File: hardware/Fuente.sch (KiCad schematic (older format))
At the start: 4 parts, among them P3 CONN_01X02, U4 NCP1117ST33T3G

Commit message: Se agrego SD, se colocaron pins en varios modulos, se corrigio orden del VGA
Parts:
- removed P3: CONN_01X02, symbol CONN_01X02
- removed U4: NCP1117ST33T3G, symbol NCP1117ST33T3G
- added U?: MCP1825S-3302E, SOT-223, symbol LM117H
- C13: value C -> 4.7uF
- C14: value C -> 1uF
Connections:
- net labels added: 3.3V_OUT, VIN
- net labels removed: +3.3V
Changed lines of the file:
@@
 LIBS:serial
 LIBS:oscillator-cmos-out-4
+LIBS:con-yamaichi-cf-2
 LIBS:STM32F4-UCC-cache
 EELAYER 24 0
@@
 $Descr A4 11693 8268
 encoding utf-8
-Sheet 5 5
+Sheet 5 6
 Title ""
 Date ""
@@
 $EndDescr
 $Comp
-L NCP1117ST33T3G U4
-U 1 1 53D551F1
-P 5350 2300
-F 0 "U4" H 5350 2550 40  0000 C CNN
-F 1 "NCP1117ST33T3G" H 5350 2500 40  0000 C CNN
-F 2 "" H 5350 2300 60  0000 C CNN
-F 3 "" H 5350 2300 60  0000 C CNN
-	1    5350 2300
-	1    0    0    -1
-$EndComp
-$Comp
 L C C14
 U 1 1 53D55294
 P 5900 2550
 F 0 "C14" H 5900 2650 40  0000 L CNN
-F 1 "C" H 5906 2465 40  0000 L CNN
+F 1 "1uF" H 5906 2465 40  0000 L CNN
 F 2 "" H 5938 2400 30  0000 C CNN
 F 3 "" H 5900 2550 60  0000 C CNN
@@
 P 4750 2550
 F 0 "C13" H 4750 2650 40  0000 L CNN
-F 1 "C" H 4756 2465 40  0000 L CNN
+F 1 "4.7uF" H 4756 2465 40  0000 L CNN
 F 2 "" H 4788 2400 30  0000 C CNN
 F 3 "" H 4750 2550 60  0000 C CNN
@@
 	1    0    0    -1
 $EndComp
-$Comp
-L CONN_01X02 P3
-U 1 1 53D55308
-P 4250 2300
-F 0 "P3" H 4250 2450 50  0000 C CNN
-F 1 "CONN_01X02" V 4350 2300 50  0000 C CNN
-F 2 "" H 4250 2300 60  0000 C CNN
-F 3 "" H 4250 2300 60  0000 C CNN
-	1    4250 2300
-	-1   0    0    1
-$EndComp
 Wire Wire Line
-	4450 2250 4950 2250
-$Comp
-L GND #PWR51
-U 1 1 53D55395
-P 4550 2450
-F 0 "#PWR51" H 4550 2450 30  0001 C CNN
-F 1 "GND" H 4550 2380 30  0001 C CNN
-F 2 "" H 4550 2450 60  0000 C CNN
-F 3 "" H 4550 2450 60  0000 C CNN
-	1    4550 2450
-	1    0    0    -1
-$EndComp
+	4550 2250 4750 2250
 Wire Wire Line
-	4450 2350 4550 2350
-Wire Wire Line
-	4550 2350 4550 2450
+	4750 2250 4950 2250
 Wire Wire Line
 	5750 2250 5900 2250
 Wire Wire Line
-	5900 2200 5900 2350
+	5900 2250 6100 2250
 Wire Wire Line
 	4750 2350 4750 2250
@@
 L GND #PWR52
 U 1 1 53D555A6
-P 4750 2850
-F 0 "#PWR52" H 4750 2850 30  0001 C CNN
-F 1 "GND" H 4750 2780 30  0001 C CNN
-F 2 "" H 4750 2850 60  0000 C CNN
-F 3 "" H 4750 2850 60  0000 C CNN
-	1    4750 2850
+P 4750 2800
+F 0 "#PWR52" H 4750 2800 30  0001 C CNN
+F 1 "GND" H 4750 2730 30  0001 C CNN
+F 2 "" H 4750 2800 60  0000 C CNN
+F 3 "" H 4750 2800 60  0000 C CNN
+	1    4750 2800
 	1    0    0    -1
 $EndComp
 Wire Wire Line
-	4750 2850 4750 2750
+	4750 2800 4750 2750
 $Comp
 L GND #PWR55
 U 1 1 53D555D6
-P 5900 2850
-F 0 "#PWR55" H 5900 2850 30  0001 C CNN
-F 1 "GND" H 5900 2780 30  0001 C CNN
-F 2 "" H 5900 2850 60  0000 C CNN
-F 3 "" H 5900 2850 60  0000 C CNN
-	1    5900 2850
+P 5900 2800
+F 0 "#PWR55" H 5900 2800 30  0001 C CNN
+F 1 "GND" H 5900 2730 30  0001 C CNN
+F 2 "" H 5900 2800 60  0000 C CNN
+F 3 "" H 5900 2800 60  0000 C CNN
+	1    5900 2800
 	1    0    0    -1
 $EndComp
 Wire Wire Line
-	5900 2850 5900 2750
+	5900 2800 5900 2750
 $Comp
 L GND #PWR53
 U 1 1 53D55626
-P 5350 2650
-F 0 "#PWR53" H 5350 2650 30  0001 C CNN
-F 1 "GND" H 5350 2580 30  0001 C CNN
-F 2 "" H 5350 2650 60  0000 C CNN
-F 3 "" H 5350 2650 60  0000 C CNN
-	1    5350 2650
+P 5350 2800
+F 0 "#PWR53" H 5350 2800 30  0001 C CNN
+F 1 "GND" H 5350 2730 30  0001 C CNN
+F 2 "" H 5350 2800 60  0000 C CNN
+F 3 "" H 5350 2800 60  0000 C CNN
+	1    5350 2800
 	1    0    0    -1
 $EndComp
 Wire Wire Line
-	5350 2650 5350 2550
+	5350 2800 5350 2550
+Connection ~ 5900 2250
 $Comp
-L +3.3V #PWR54
-U 1 1 53D55633
-P 5900 2200
-F 0 "#PWR54" H 5900 2160 30  0001 C CNN
-F 1 "+3.3V" H 5900 2310 30  0000 C CNN
-F 2 "" H 5900 2200 60  0000 C CNN
-F 3 "" H 5900 2200 60  0000 C CNN
-	1    5900 2200
+L LM117H U?
+U 1 1 53DE486A
+P 5350 2300
+F 0 "U?" H 5150 2100 40  0000 C CNN
+F 1 "MCP1825S-3302E" H 5100 2500 40  0000 L CNN
+F 2 "SOT-223" H 5350 2400 30  0000 C CIN
+F 3 "" H 5350 2300 60  0000 C CNN
+	1    5350 2300
 	1    0    0    -1
 $EndComp
-Connection ~ 5900 2250
+Text HLabel 6100 2250 2    40   Input ~ 0
+3.3V_OUT
+Wire Wire Line
+	5900 2350 5900 2250
+Text HLabel 4550 2250 0    40   Input ~ 0
+VIN
 $EndSCHEMATC

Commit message: Terminado el esquematico, iniciado el PCB
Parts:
- removed U?: MCP1825S-3302E, SOT-223, symbol LM117H
- added U4: MSP1825S-3302E, SMD_Packages:SOT-223, symbol MSP1825S-3302E
- C13, C14: footprint (none) -> Capacitors_ThroughHole:Capacitor5x11RM2.5
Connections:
- net 3.3V_OUT: now also U4.3 (OUT)
- net GND: now also U4.2 (ADJ), U4.4 (gnd)
- net VIN: now also U4.1 (IN)
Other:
- moved on the sheet: C13, C14
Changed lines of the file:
@@
 L C C14
 U 1 1 53D55294
-P 5900 2550
-F 0 "C14" H 5900 2650 40  0000 L CNN
-F 1 "1uF" H 5906 2465 40  0000 L CNN
-F 2 "" H 5938 2400 30  0000 C CNN
-F 3 "" H 5900 2550 60  0000 C CNN
-	1    5900 2550
+P 6350 3850
+F 0 "C14" H 6350 3950 40  0000 L CNN
+F 1 "1uF" H 6356 3765 40  0000 L CNN
+F 2 "Capacitors_ThroughHole:Capacitor5x11RM2.5" H 6388 3700 30  0001 C CNN
+F 3 "" H 6350 3850 60  0000 C CNN
+	1    6350 3850
 	1    0    0    -1
 $EndComp
@@
 L C C13
 U 1 1 53D552E9
-P 4750 2550
-F 0 "C13" H 4750 2650 40  0000 L CNN
-F 1 "4.7uF" H 4756 2465 40  0000 L CNN
-F 2 "" H 4788 2400 30  0000 C CNN
-F 3 "" H 4750 2550 60  0000 C CNN
-	1    4750 2550
+P 5200 3850
+F 0 "C13" H 5200 3950 40  0000 L CNN
+F 1 "4.7uF" H 5206 3765 40  0000 L CNN
+F 2 "Capacitors_ThroughHole:Capacitor5x11RM2.5" H 5238 3700 30  0001 C CNN
+F 3 "" H 5200 3850 60  0000 C CNN
+	1    5200 3850
 	1    0    0    -1
 $EndComp
 Wire Wire Line
-	4550 2250 4750 2250
+	5000 3550 5400 3550
 Wire Wire Line
-	4750 2250 4950 2250
+	6200 3550 6550 3550
 Wire Wire Line
-	5750 2250 5900 2250
-Wire Wire Line
-	5900 2250 6100 2250
-Wire Wire Line
-	4750 2350 4750 2250
-Connection ~ 4750 2250
+	5200 3650 5200 3550
+Connection ~ 5200 3550
 $Comp
-L GND #PWR52
+L GND #PWR051
 U 1 1 53D555A6
-P 4750 2800
-F 0 "#PWR52" H 4750 2800 30  0001 C CNN
-F 1 "GND" H 4750 2730 30  0001 C CNN
-F 2 "" H 4750 2800 60  0000 C CNN
-F 3 "" H 4750 2800 60  0000 C CNN
-	1    4750 2800
+P 5200 4100
+F 0 "#PWR051" H 5200 4100 30  0001 C CNN
+F 1 "GND" H 5200 4030 30  0001 C CNN
+F 2 "" H 5200 4100 60  0000 C CNN
+F 3 "" H 5200 4100 60  0000 C CNN
+	1    5200 4100
 	1    0    0    -1
 $EndComp
 Wire Wire Line
-	4750 2800 4750 2750
+	5200 4100 5200 4050
 $Comp
-L GND #PWR55
+L GND #PWR052
 U 1 1 53D555D6
-P 5900 2800
-F 0 "#PWR55" H 5900 2800 30  0001 C CNN
-F 1 "GND" H 5900 2730 30  0001 C CNN
-F 2 "" H 5900 2800 60  0000 C CNN
-F 3 "" H 5900 2800 60  0000 C CNN
-	1    5900 2800
+P 6350 4100
+F 0 "#PWR052" H 6350 4100 30  0001 C CNN
+F 1 "GND" H 6350 4030 30  0001 C CNN
+F 2 "" H 6350 4100 60  0000 C CNN
+F 3 "" H 6350 4100 60  0000 C CNN
+	1    6350 4100
 	1    0    0    -1
 $EndComp
 Wire Wire Line
-	5900 2800 5900 2750
+	6350 4100 6350 4050
 $Comp
-L GND #PWR53
+L GND #PWR053
 U 1 1 53D55626
-P 5350 2800
-F 0 "#PWR53" H 5350 2800 30  0001 C CNN
-F 1 "GND" H 5350 2730 30  0001 C CNN
-F 2 "" H 5350 2800 60  0000 C CNN
-F 3 "" H 5350 2800 60  0000 C CNN
-	1    5350 2800
+P 5800 4100
+F 0 "#PWR053" H 5800 4100 30  0001 C CNN
+F 1 "GND" H 5800 4030 30  0001 C CNN
+F 2 "" H 5800 4100 60  0000 C CNN
+F 3 "" H 5800 4100 60  0000 C CNN
+	1    5800 4100
 	1    0    0    -1
 $EndComp
+Connection ~ 6350 3550
+Text HLabel 6550 3550 2    40   Input ~ 0
+3.3V_OUT
 Wire Wire Line
-	5350 2800 5350 2550
-Connection ~ 5900 2250
+	6350 3650 6350 3550
+Text HLabel 5000 3550 0    40   Input ~ 0
+VIN
+Wire Wire Line
+	5850 3850 5850 3900
+Wire Wire Line
+	5850 3900 5750 3900
+Wire Wire Line
+	5750 3900 5750 3850
+Wire Wire Line
+	5800 3900 5800 4100
+Connection ~ 5800 3900
 $Comp
-L LM117H U?
-U 1 1 53DE486A
-P 5350 2300
-F 0 "U?" H 5150 2100 40  0000 C CNN
-F 1 "MCP1825S-3302E" H 5100 2500 40  0000 L CNN
-F 2 "SOT-223" H 5350 2400 30  0000 C CIN
-F 3 "" H 5350 2300 60  0000 C CNN
-	1    5350 2300
+L MSP1825S-3302E U4
+U 1 1 53E687BD
+P 5800 3600
+F 0 "U4" H 5600 3800 40  0000 C CNN
+F 1 "MSP1825S-3302E" H 5800 3800 40  0000 L CNN
+F 2 "SMD_Packages:SOT-223" H 5800 3700 30  0000 C CIN
+F 3 "" H 5800 3600 60  0000 C CNN
+	1    5800 3600
 	1    0    0    -1
 $EndComp
-Text HLabel 6100 2250 2    40   Input ~ 0
-3.3V_OUT
-Wire Wire Line
-	5900 2350 5900 2250
-Text HLabel 4550 2250 0    40   Input ~ 0
-VIN
 $EndSCHEMATC

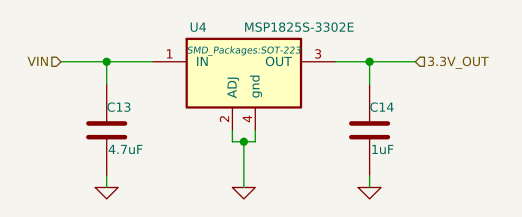
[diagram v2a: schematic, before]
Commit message: Terminado el Routeo de la Placa
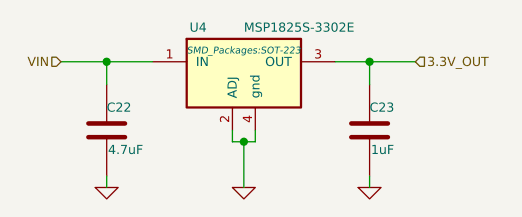
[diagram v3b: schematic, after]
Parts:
- renumbered C13 to C22, C14 to C23
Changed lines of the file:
@@
 LIBS:oscillator-cmos-out-4
 LIBS:con-yamaichi-cf-2
+LIBS:w_connectors
 LIBS:STM32F4-UCC-cache
 EELAYER 24 0
@@
 $EndDescr
 $Comp
-L C C14
+L C C23
 U 1 1 53D55294
 P 6350 3850
-F 0 "C14" H 6350 3950 40  0000 L CNN
+F 0 "C23" H 6350 3950 40  0000 L CNN
 F 1 "1uF" H 6356 3765 40  0000 L CNN
 F 2 "Capacitors_ThroughHole:Capacitor5x11RM2.5" H 6388 3700 30  0001 C CNN
@@
 $EndComp
 $Comp
-L C C13
+L C C22
 U 1 1 53D552E9
 P 5200 3850
-F 0 "C13" H 5200 3950 40  0000 L CNN
+F 0 "C22" H 5200 3950 40  0000 L CNN
 F 1 "4.7uF" H 5206 3765 40  0000 L CNN
 F 2 "Capacitors_ThroughHole:Capacitor5x11RM2.5" H 5238 3700 30  0001 C CNN
@@
 Connection ~ 5200 3550
 $Comp
-L GND #PWR051
+L GND #PWR044
 U 1 1 53D555A6
 P 5200 4100
-F 0 "#PWR051" H 5200 4100 30  0001 C CNN
+F 0 "#PWR044" H 5200 4100 30  0001 C CNN
 F 1 "GND" H 5200 4030 30  0001 C CNN
 F 2 "" H 5200 4100 60  0000 C CNN
@@
 	5200 4100 5200 4050
 $Comp
-L GND #PWR052
+L GND #PWR045
 U 1 1 53D555D6
 P 6350 4100
-F 0 "#PWR052" H 6350 4100 30  0001 C CNN
+F 0 "#PWR045" H 6350 4100 30  0001 C CNN
 F 1 "GND" H 6350 4030 30  0001 C CNN
 F 2 "" H 6350 4100 60  0000 C CNN
@@
 	6350 4100 6350 4050
 $Comp
-L GND #PWR053
+L GND #PWR046
 U 1 1 53D55626
 P 5800 4100
-F 0 "#PWR053" H 5800 4100 30  0001 C CNN
+F 0 "#PWR046" H 5800 4100 30  0001 C CNN
 F 1 "GND" H 5800 4030 30  0001 C CNN
 F 2 "" H 5800 4100 60  0000 C CNN

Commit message: Placa terminada, serigrafia verificada, logos agregados
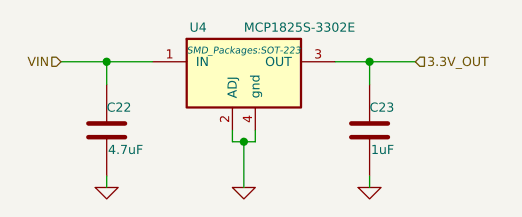
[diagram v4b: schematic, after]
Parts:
- U4: value MSP1825S-3302E -> MCP1825S-3302E
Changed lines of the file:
@@
 P 5800 3600
 F 0 "U4" H 5600 3800 40  0000 C CNN
-F 1 "MSP1825S-3302E" H 5800 3800 40  0000 L CNN
+F 1 "MCP1825S-3302E" H 5800 3800 40  0000 L CNN
 F 2 "SMD_Packages:SOT-223" H 5800 3700 30  0000 C CIN
 F 3 "" H 5800 3600 60  0000 C CNN
